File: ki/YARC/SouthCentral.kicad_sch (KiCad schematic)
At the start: 8 parts, among them U83 74LS139, U84 74LS157, U85 74LS157, U86 74LS157, U87 74LS138, U88 74HC00, U89 74LS157, U90 74LS157

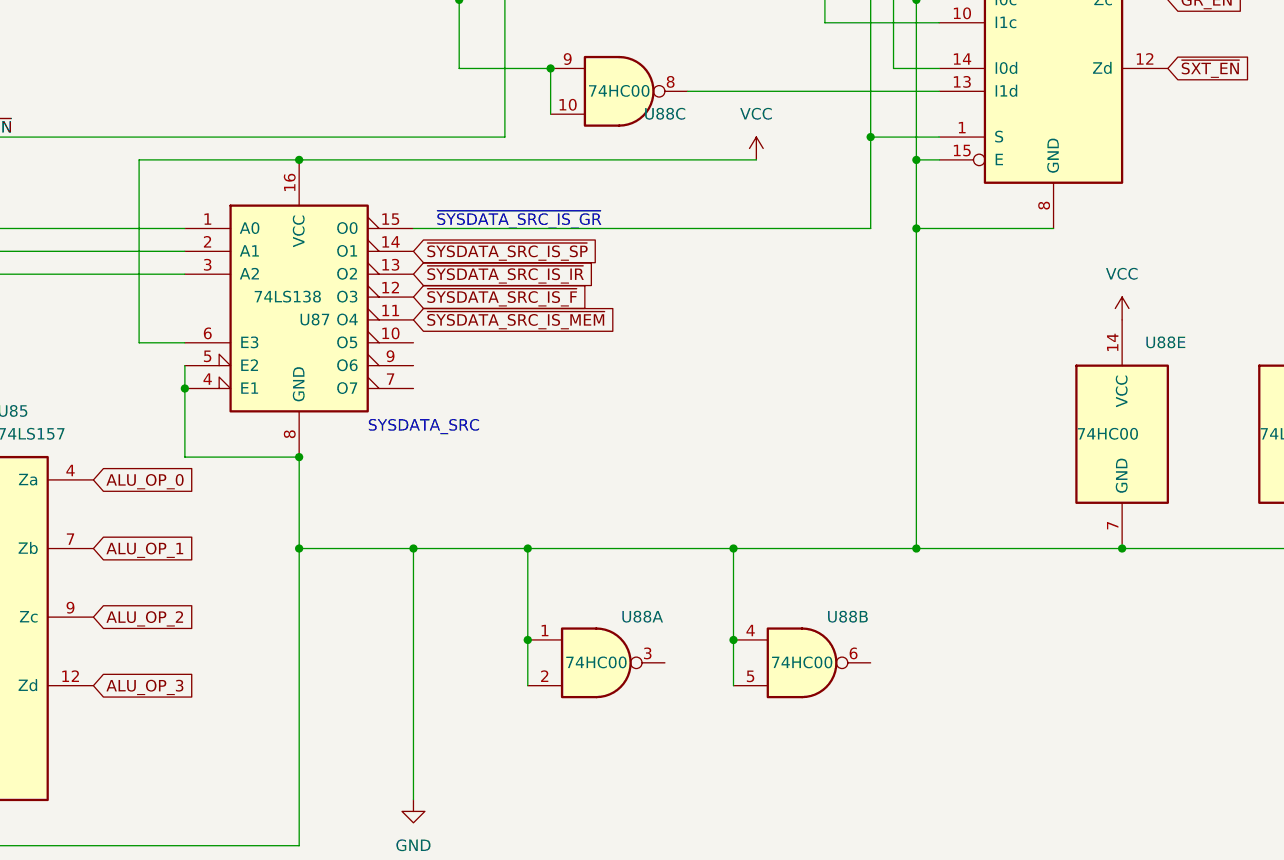
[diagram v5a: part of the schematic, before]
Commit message: Flags development and implement memory fix. Firmware not updated to match the memory fix.
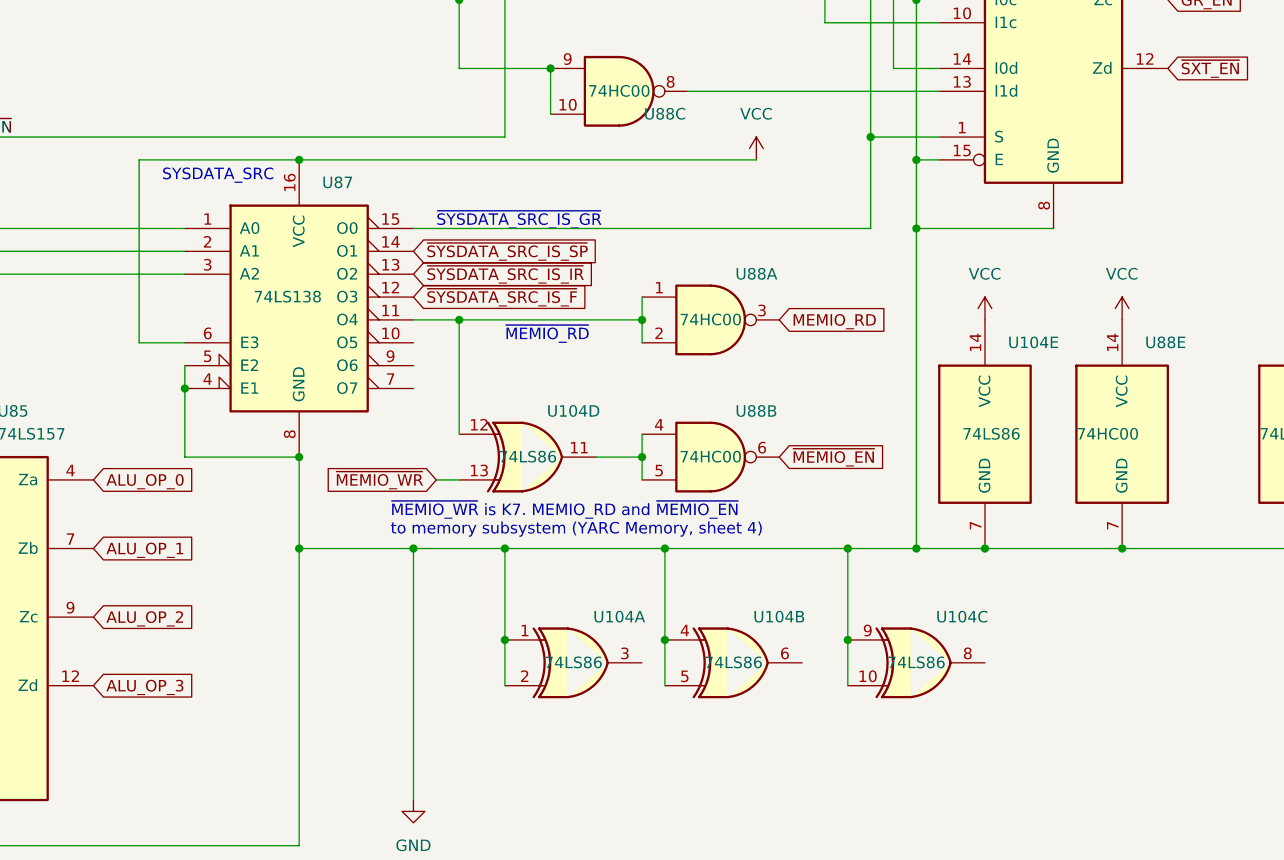
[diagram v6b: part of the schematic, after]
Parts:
- added U104: 74LS86, symbol 74xx:74LS86
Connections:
- net GND: now also U104.1, U104.10, U104.2, U104.4, U104.5, U104.7 (GND), U104.9; no longer U88.1, U88.2, U88.4, U88.5
- net VCC: now also U104.14 (VCC)
- net ~{MEMIO_EN}: now reaches U88.6
- net MEMIO_RD: now reaches U88.3
- net ~{SYSDATA_SRC_IS_MEM}: no longer names the net of U87.11 (O4)
- net ~{SYSDATA_SRC_IS_MEM}: now also U88.1, U88.2, U104.12
- new net: U104.11, U88.4, U88.5
- new net ~{MEMIO_WR}: U104.13
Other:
- note added: "~{MEMIO_RD}"
- note added: "~{MEMIO_WR} is K7. MEMIO_RD and ~{MEMIO_EN} to memory subsystem (YARC Memory, sheet 4)"
- moved on the sheet: U88A, U88B

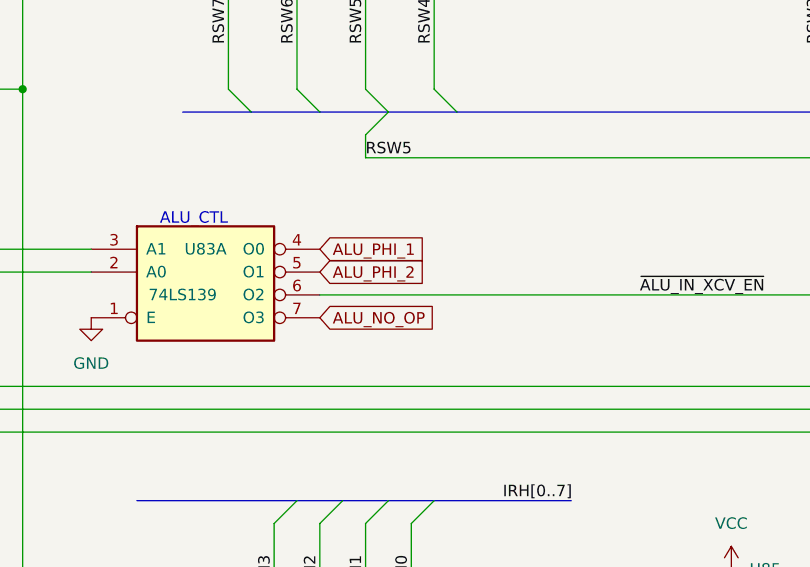
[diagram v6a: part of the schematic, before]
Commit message: Major changes to ALU, Flags, and add new ALU controls schematic
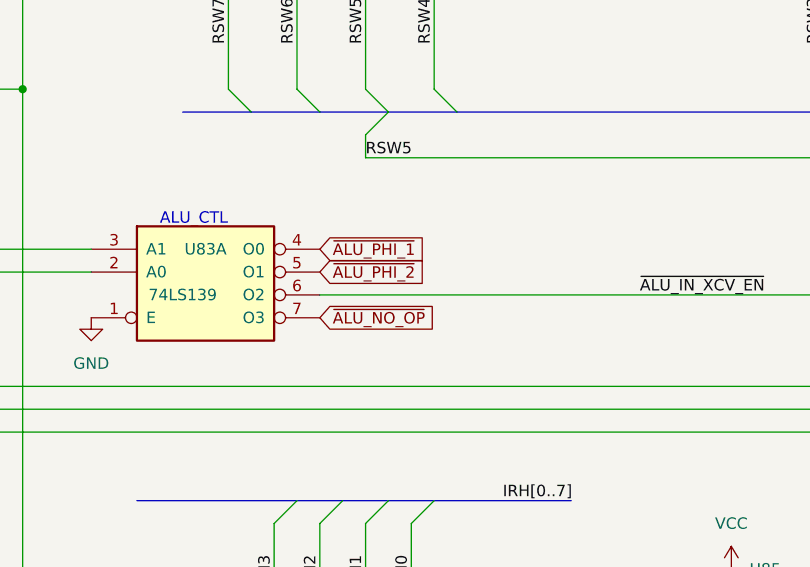
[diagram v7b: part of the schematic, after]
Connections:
- net ALU_NO_OP renamed ~{ALU_NO_OP}
- net ALU_PHI_1 renamed ~{ALU_PHI_1}
- net ALU_PHI_2 renamed ~{ALU_PHI_2}
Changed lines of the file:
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@@
     )
   )
-  (global_label "ALU_NO_OP" (shape input) (at 60.96 124.46 0) (fields_autoplaced)
+  (global_label "~{ALU_NO_OP}" (shape input) (at 60.96 124.46 0) (fields_autoplaced)
     (effects (font (size 1.27 1.27)) (justify left))
     (property "Intersheet References" "${INTERSHEET_REFS}" (id 0) (at 74.0169 124.3806 0)
@@
     )
   )
-  (global_label "ALU_PHI_1" (shape input) (at 60.96 116.84 0) (fields_autoplaced)
+  (global_label "~{ALU_PHI_1}" (shape input) (at 60.96 116.84 0) (fields_autoplaced)
     (effects (font (size 1.27 1.27)) (justify left))
     (property "Intersheet References" "${INTERSHEET_REFS}" (id 0) (at 73.1702 116.7606 0)
@@
     )
   )
-  (global_label "ALU_PHI_2" (shape input) (at 60.96 119.38 0) (fields_autoplaced)
+  (global_label "~{ALU_PHI_2}" (shape input) (at 60.96 119.38 0) (fields_autoplaced)
     (effects (font (size 1.27 1.27)) (justify left))
     (property "Intersheet References" "${INTERSHEET_REFS}" (id 0) (at 73.1702 119.3006 0)

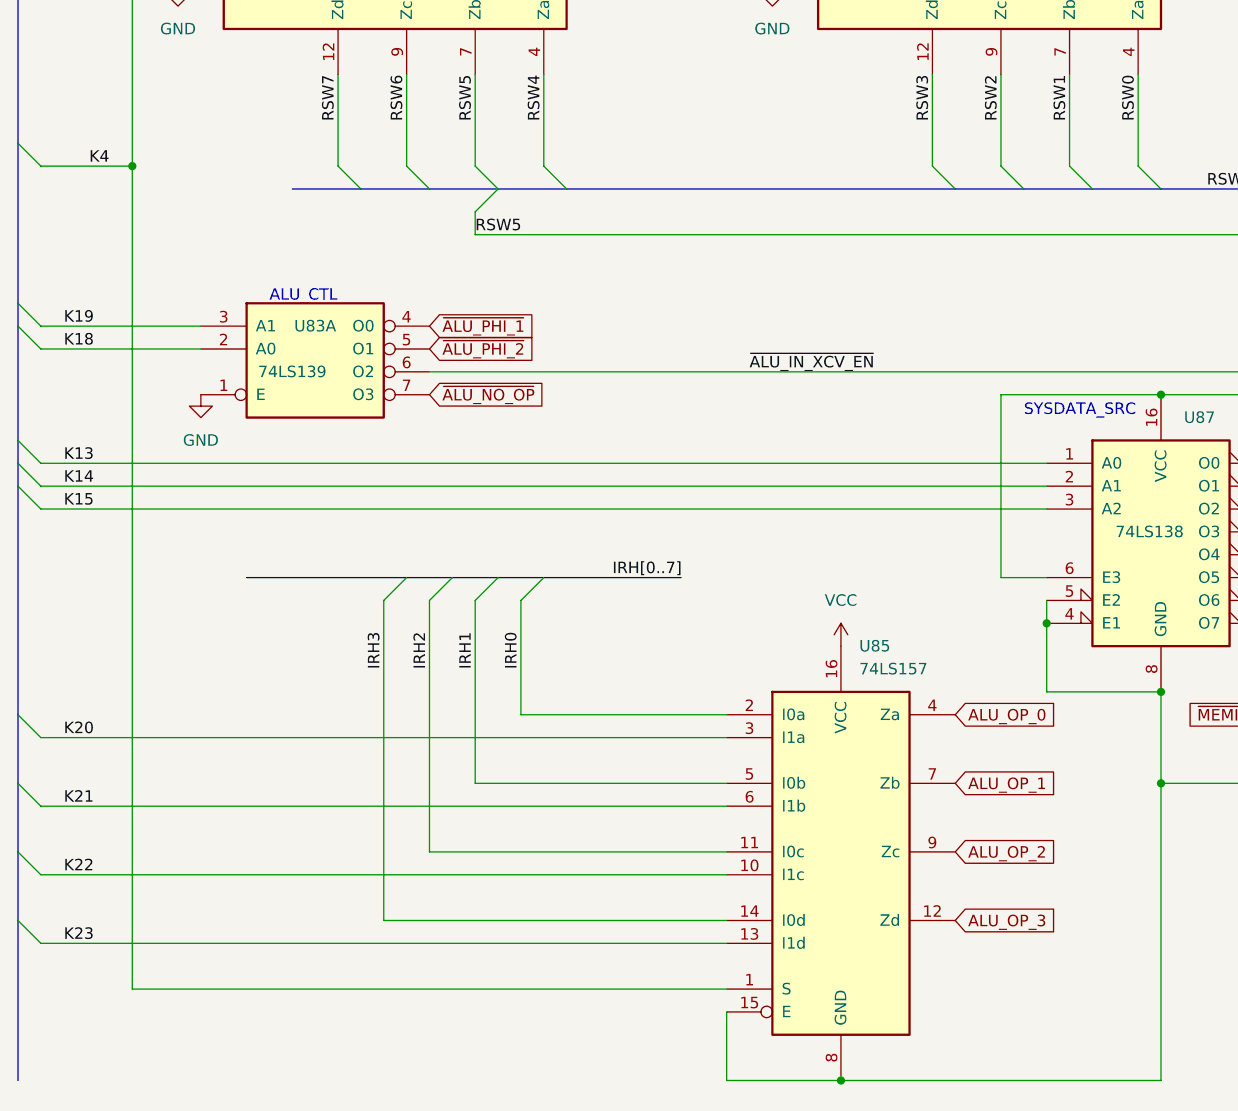
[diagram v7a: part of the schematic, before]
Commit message: Discovered that ACN mux was already drawn on another sheet of the schematic - fixed. Added ACN control bit to microcode. Ongoing cleanup: replaced acronym RSW with RCW in assembly language.
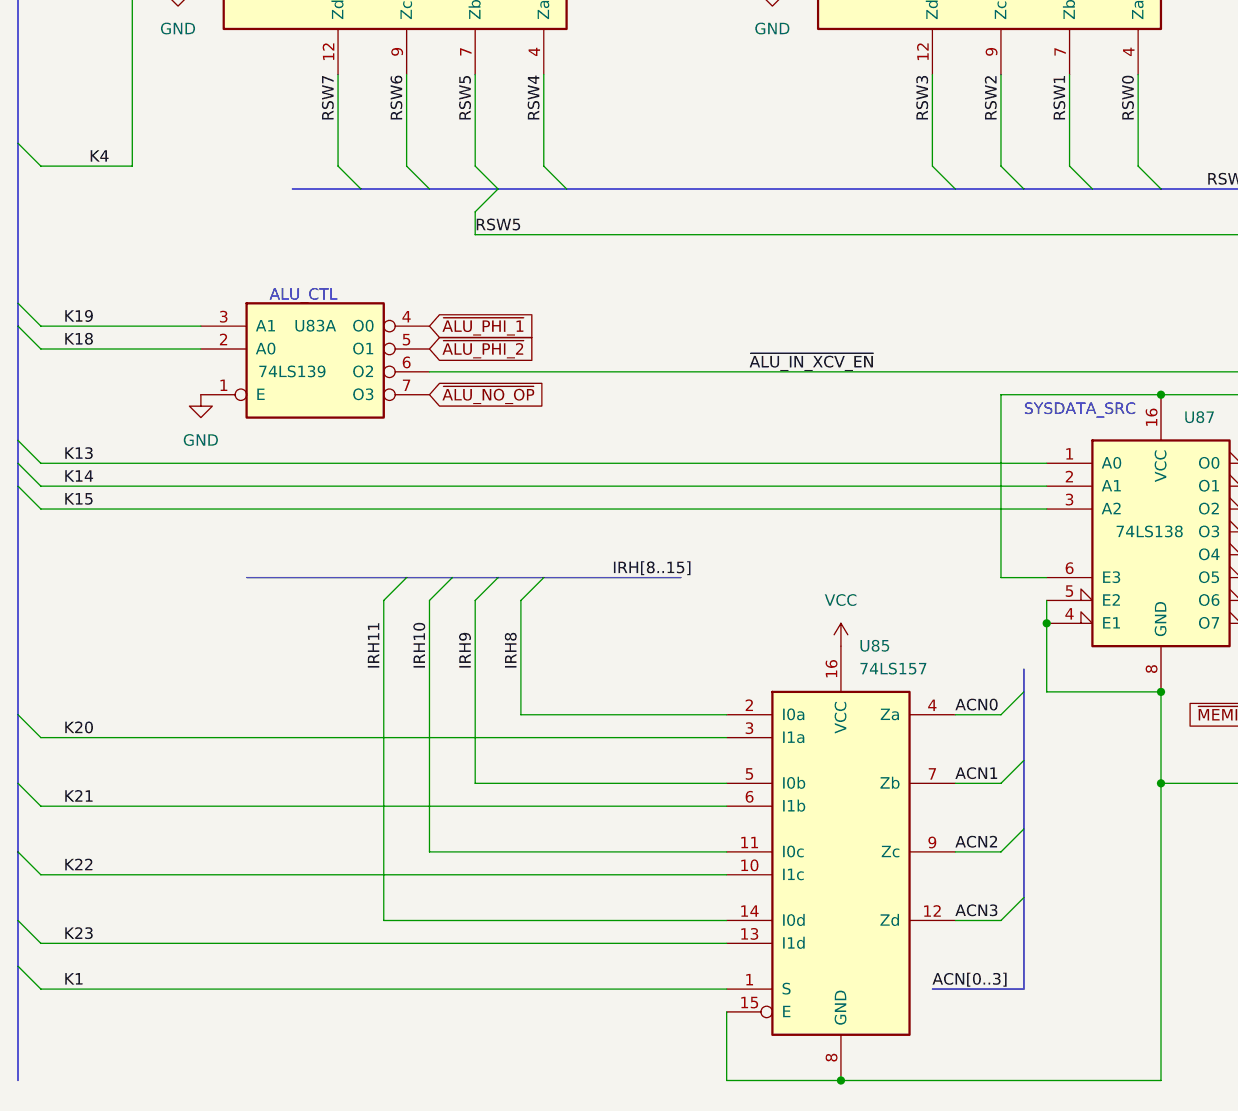
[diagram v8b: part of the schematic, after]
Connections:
- net K4: no longer U85.1 (S)
- net ALU_OP_0 renamed ACN0
- net ALU_OP_1 renamed ACN1
- net ALU_OP_2 renamed ACN2
- net ALU_OP_3 renamed ACN3
- net IRH0 renamed IRH8
- net IRH1 renamed IRH9
- net IRH2 renamed IRH10
- net IRH3 renamed IRH11
- new net K1: U85.1 (S)
